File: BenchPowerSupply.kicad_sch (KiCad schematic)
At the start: 2 parts

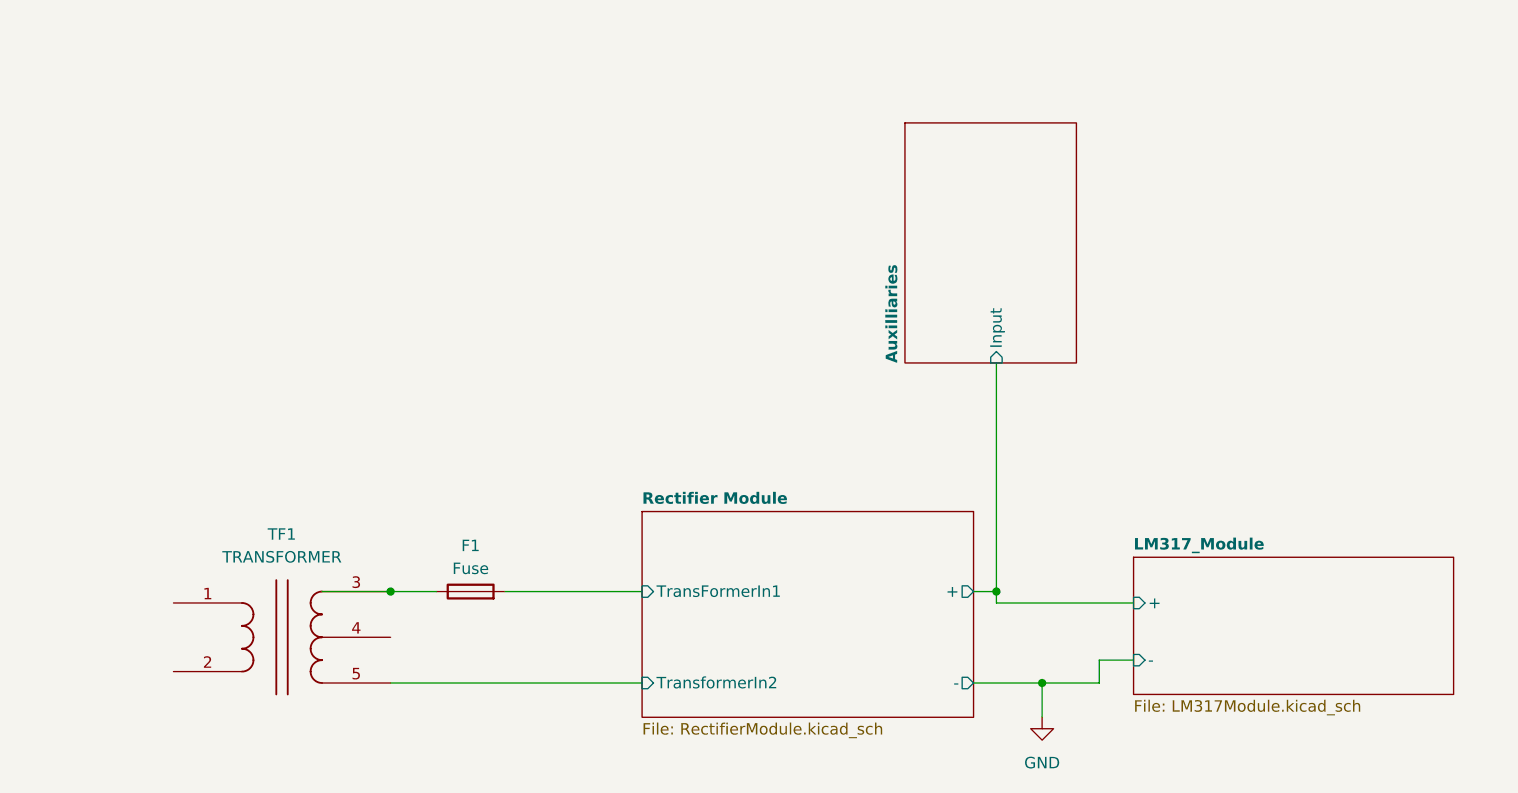
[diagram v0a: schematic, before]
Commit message: Updates to the schematic to make use of the centre tapped transformer to get negative rail.
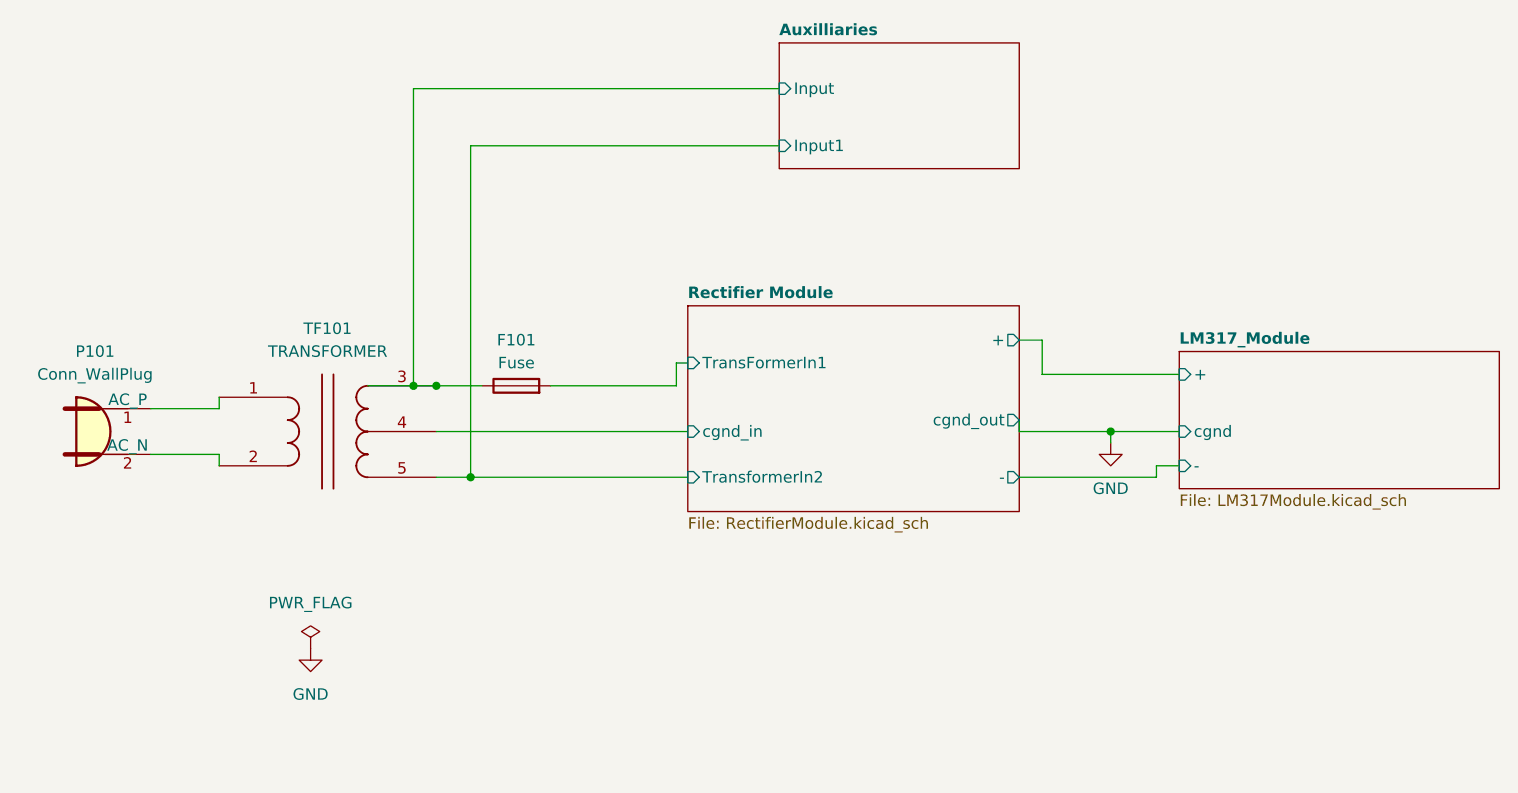
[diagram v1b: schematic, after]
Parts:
- added P101: Conn_WallPlug, symbol Connector:Conn_WallPlug
- renumbered F1 to F101, TF1 to TF101
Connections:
- net Auxilliaries/Input: now also F101.1, TF101.3
- net at TF101.1: now also P101.1 (AC_P)
- net at TF101.2: now also P101.2 (AC_N)
- net Rectifier Module/cgnd_in: now reaches TF101.4
- net Rectifier Module/TransformerIn2 renamed Auxilliaries/Input1
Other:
- sheet Auxilliaries ports: added Input1; removed none
- sheet LM317_Module ports: added cgnd; removed none
- sheet Rectifier Module ports: added cgnd_in, cgnd_out; removed none
- moved on the sheet: F101, TF101
